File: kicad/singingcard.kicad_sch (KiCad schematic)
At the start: 16 parts, among them J2 Audio_In, SW1 Button, U1 ISD3900FYI, U2 W25Q16JVSSIQ

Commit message: Fix global label orientation - flags point toward component
- Remove incorrect 180° flip from label angle calculation
- Label flags now point toward component (same direction as pin angle)
- Left-side pins: flag points right, text extends left
- Right-side pins: flag points left, text extends right
- Wires connect to flag tip, not through label text

🤖 Generated with [Claude Code](https://claude.com/claude-code)

Co-Authored-By: Claude <noreply@anthropic.com>
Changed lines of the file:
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@@
 		(instances
 			(project "singingcard"
-				(path "/7b994266-04b8-4378-91cb-6096748c65af"
+				(path "/6c95bb3a-6328-4d30-b137-739b35f84dae"
 					(reference "U1")
 					(unit 1)
@@
 		(instances
 			(project "singingcard"
-				(path "/7b994266-04b8-4378-91cb-6096748c65af"
+				(path "/6c95bb3a-6328-4d30-b137-739b35f84dae"
 					(reference "U2")
 					(unit 1)
@@
 		(instances
 			(project "singingcard"
-				(path "/7b994266-04b8-4378-91cb-6096748c65af"
+				(path "/6c95bb3a-6328-4d30-b137-739b35f84dae"
 					(reference "BT1")
 					(unit 1)
@@
 		(instances
 			(project "singingcard"
-				(path "/7b994266-04b8-4378-91cb-6096748c65af"
+				(path "/6c95bb3a-6328-4d30-b137-739b35f84dae"
 					(reference "R1")
 					(unit 1)
@@
 		(instances
 			(project "singingcard"
-				(path "/7b994266-04b8-4378-91cb-6096748c65af"
+				(path "/6c95bb3a-6328-4d30-b137-739b35f84dae"
 					(reference "R2")
 					(unit 1)
@@
 		(instances
 			(project "singingcard"
-				(path "/7b994266-04b8-4378-91cb-6096748c65af"
+				(path "/6c95bb3a-6328-4d30-b137-739b35f84dae"
 					(reference "R3")
 					(unit 1)
@@
 		(instances
 			(project "singingcard"
-				(path "/7b994266-04b8-4378-91cb-6096748c65af"
+				(path "/6c95bb3a-6328-4d30-b137-739b35f84dae"
 					(reference "R4")
 					(unit 1)
@@
 		(instances
 			(project "singingcard"
-				(path "/7b994266-04b8-4378-91cb-6096748c65af"
+				(path "/6c95bb3a-6328-4d30-b137-739b35f84dae"
 					(reference "C1")
 					(unit 1)
@@
 		(instances
 			(project "singingcard"
-				(path "/7b994266-04b8-4378-91cb-6096748c65af"
+				(path "/6c95bb3a-6328-4d30-b137-739b35f84dae"
 					(reference "C2")
 					(unit 1)
@@
 		(instances
 			(project "singingcard"
-				(path "/7b994266-04b8-4378-91cb-6096748c65af"
+				(path "/6c95bb3a-6328-4d30-b137-739b35f84dae"
 					(reference "C3")
 					(unit 1)
@@
 		(instances
 			(project "singingcard"
-				(path "/7b994266-04b8-4378-91cb-6096748c65af"
+				(path "/6c95bb3a-6328-4d30-b137-739b35f84dae"
 					(reference "C4")
 					(unit 1)
@@
 		(instances
 			(project "singingcard"
-				(path "/7b994266-04b8-4378-91cb-6096748c65af"
+				(path "/6c95bb3a-6328-4d30-b137-739b35f84dae"
 					(reference "C5")
 					(unit 1)
@@
 		(instances
 			(project "singingcard"
-				(path "/7b994266-04b8-4378-91cb-6096748c65af"
+				(path "/6c95bb3a-6328-4d30-b137-739b35f84dae"
 					(reference "C6")
 					(unit 1)
@@
 		(instances
 			(project "singingcard"
-				(path "/7b994266-04b8-4378-91cb-6096748c65af"
+				(path "/6c95bb3a-6328-4d30-b137-739b35f84dae"
 					(reference "LS1")
 					(unit 1)
@@
 		(instances
 			(project "singingcard"
-				(path "/7b994266-04b8-4378-91cb-6096748c65af"
+				(path "/6c95bb3a-6328-4d30-b137-739b35f84dae"
 					(reference "J2")
 					(unit 1)
@@
 		(instances
 			(project "singingcard"
-				(path "/7b994266-04b8-4378-91cb-6096748c65af"
+				(path "/6c95bb3a-6328-4d30-b137-739b35f84dae"
 					(reference "SW1")
 					(unit 1)
@@
 	(global_label "+3V"
 		(shape bidirectional)
-		(at 157.48 156.21 180)
+		(at 157.48 156.21 0)
 		(effects
 			(font
@@
 	(global_label "+3V"
 		(shape bidirectional)
-		(at 144.78 153.67 180)
+		(at 144.78 153.67 0)
 		(effects
 			(font
@@
 	(global_label "+3V"
 		(shape bidirectional)
-		(at 182.88 130.81 180)
+		(at 182.88 130.81 0)
 		(effects
 			(font
@@
 	(global_label "+3V"
 		(shape bidirectional)
-		(at 347.98 123.19 0)
+		(at 347.98 123.19 180)
 		(effects
 			(font
@@
 	(global_label "+3V"
 		(shape bidirectional)
-		(at 274.32 118.11 180)
+		(at 274.32 118.11 0)
 		(effects
 			(font
@@
 	(global_label "+3V"
 		(shape bidirectional)
-		(at 386.08 120.65 0)
+		(at 386.08 120.65 180)
 		(effects
 			(font
@@
 	(global_label "GND"
 		(shape bidirectional)
-		(at 182.88 140.97 180)
+		(at 182.88 140.97 0)
 		(effects
 			(font
@@
 	(global_label "GND"
 		(shape bidirectional)
-		(at 312.42 115.57 180)
+		(at 312.42 115.57 0)
 		(effects
 			(font
@@
 	(global_label "GPIO0"
 		(shape bidirectional)
-		(at 170.18 128.27 180)
+		(at 170.18 128.27 0)
 		(effects
 			(font
@@
 	(global_label "GPIO1"
 		(shape bidirectional)
-		(at 256.54 125.73 0)
+		(at 256.54 125.73 180)
 		(effects
 			(font
@@
 	(global_label "GPIO2"
 		(shape bidirectional)
-		(at 256.54 135.89 0)
+		(at 256.54 135.89 180)
 		(effects
 			(font
@@
 	(global_label "RESET"
 		(shape bidirectional)
-		(at 182.88 151.13 180)
+		(at 182.88 151.13 0)
 		(effects
 			(font
@@
 	(global_label "SPI_CS"
 		(shape bidirectional)
-		(at 243.84 153.67 0)
+		(at 243.84 153.67 180)
 		(effects
 			(font
@@
 	(global_label "SPI_CS"
 		(shape bidirectional)
-		(at 299.72 123.19 180)
+		(at 299.72 123.19 0)
 		(effects
 			(font
@@
 	(global_label "SPI_MOSI"
 		(shape bidirectional)
-		(at 256.54 166.37 0)
+		(at 256.54 166.37 180)
 		(effects
 			(font
@@
 	(global_label "SPI_MOSI"
 		(shape bidirectional)
-		(at 360.68 115.57 0)
+		(at 360.68 115.57 180)
 		(effects
 			(font
@@
 	(global_label "SPI_MISO"
 		(shape bidirectional)
-		(at 218.44 168.91 0)
+		(at 218.44 168.91 180)
 		(effects
 			(font
@@
 	(global_label "SPI_MISO"
 		(shape bidirectional)
-		(at 287.02 120.65 180)
+		(at 287.02 120.65 0)
 		(effects
 			(font
@@
 	(global_label "SPI_CLK"
 		(shape bidirectional)
-		(at 218.44 138.43 0)
+		(at 218.44 138.43 180)
 		(effects
 			(font
@@
 	(global_label "SPI_CLK"
 		(shape bidirectional)
-		(at 373.38 118.11 0)
+		(at 373.38 118.11 180)
 		(effects
 			(font
@@
 	(global_label "SP+"
 		(shape bidirectional)
-		(at 170.18 138.43 180)
+		(at 170.18 138.43 0)
 		(effects
 			(font
@@
 	(global_label "SP-"
 		(shape bidirectional)
-		(at 157.48 135.89 180)
+		(at 157.48 135.89 0)
 		(effects
 			(font
@@
 	(global_label "ANA_IN+"
 		(shape bidirectional)
-		(at 157.48 146.05 180)
+		(at 157.48 146.05 0)
 		(effects
 			(font
@@
 	(global_label "ANA_IN-"
 		(shape bidirectional)
-		(at 144.78 143.51 180)
-		(effects
-			(font
+		(at 144.78 143.51 0)
+		(effects
+			(font

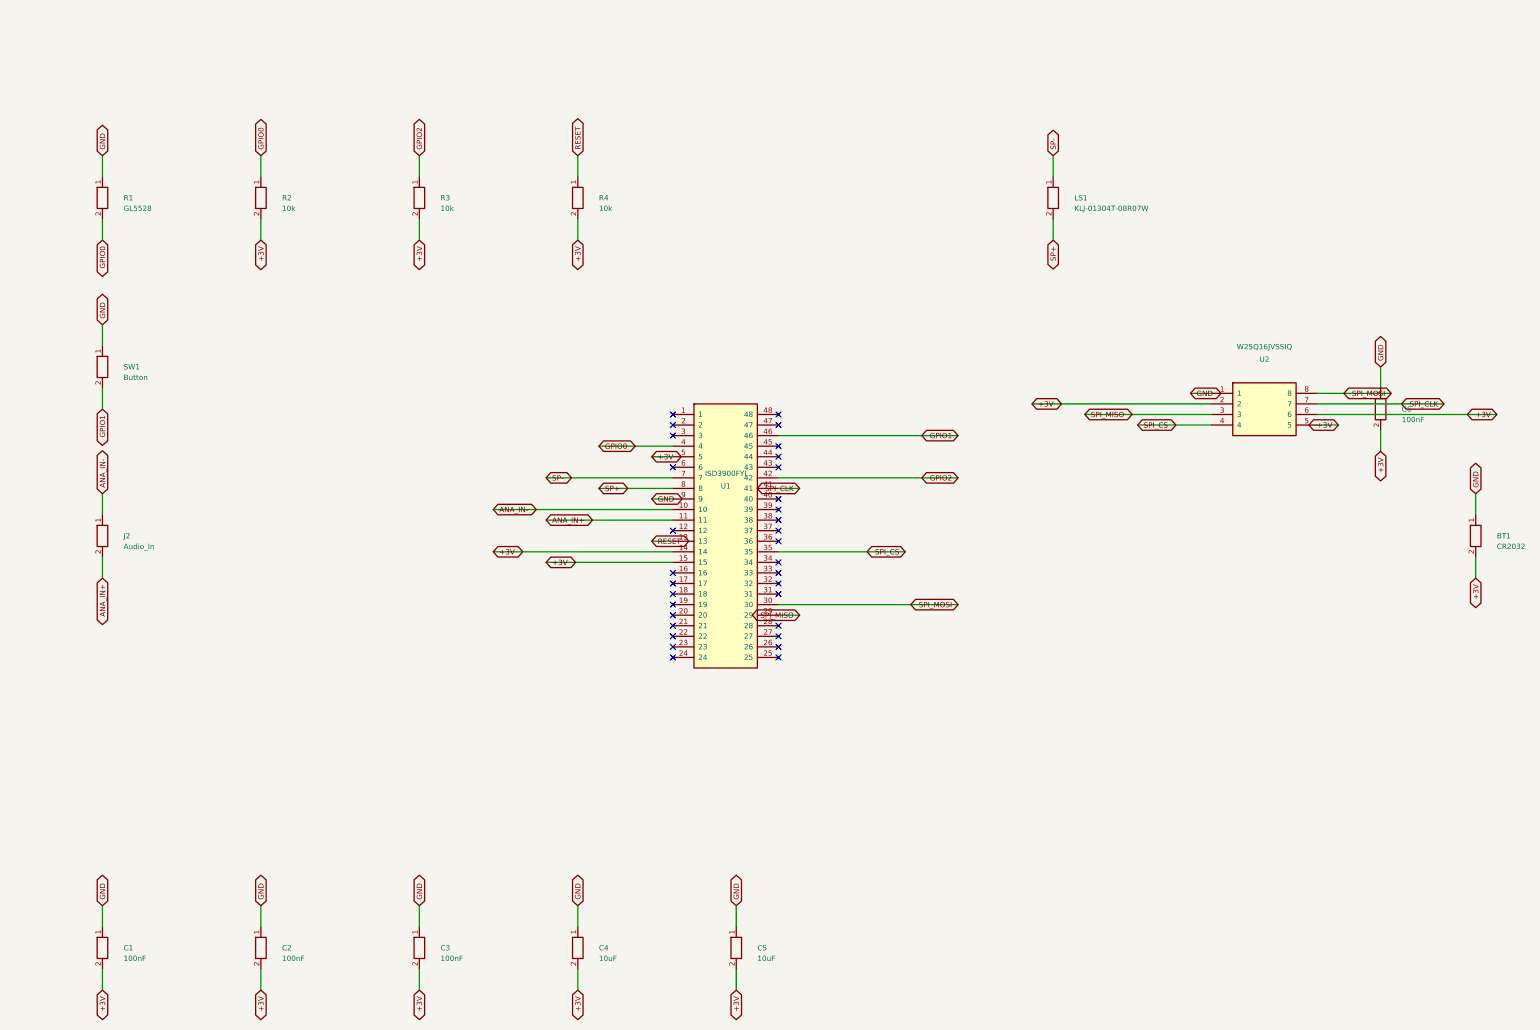
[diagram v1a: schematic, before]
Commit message: Compact schematic layout on A4, labels directly on pins
- Change from A3 to A4 page size
- Compact component positions for tighter layout
- Place labels directly at pin positions (no wires)
- Label angles opposite to pin direction so text extends away from components
- Much cleaner appearance without wire-through-label issues

🤖 Generated with [Claude Code](https://claude.com/claude-code)

Co-Authored-By: Claude <noreply@anthropic.com>
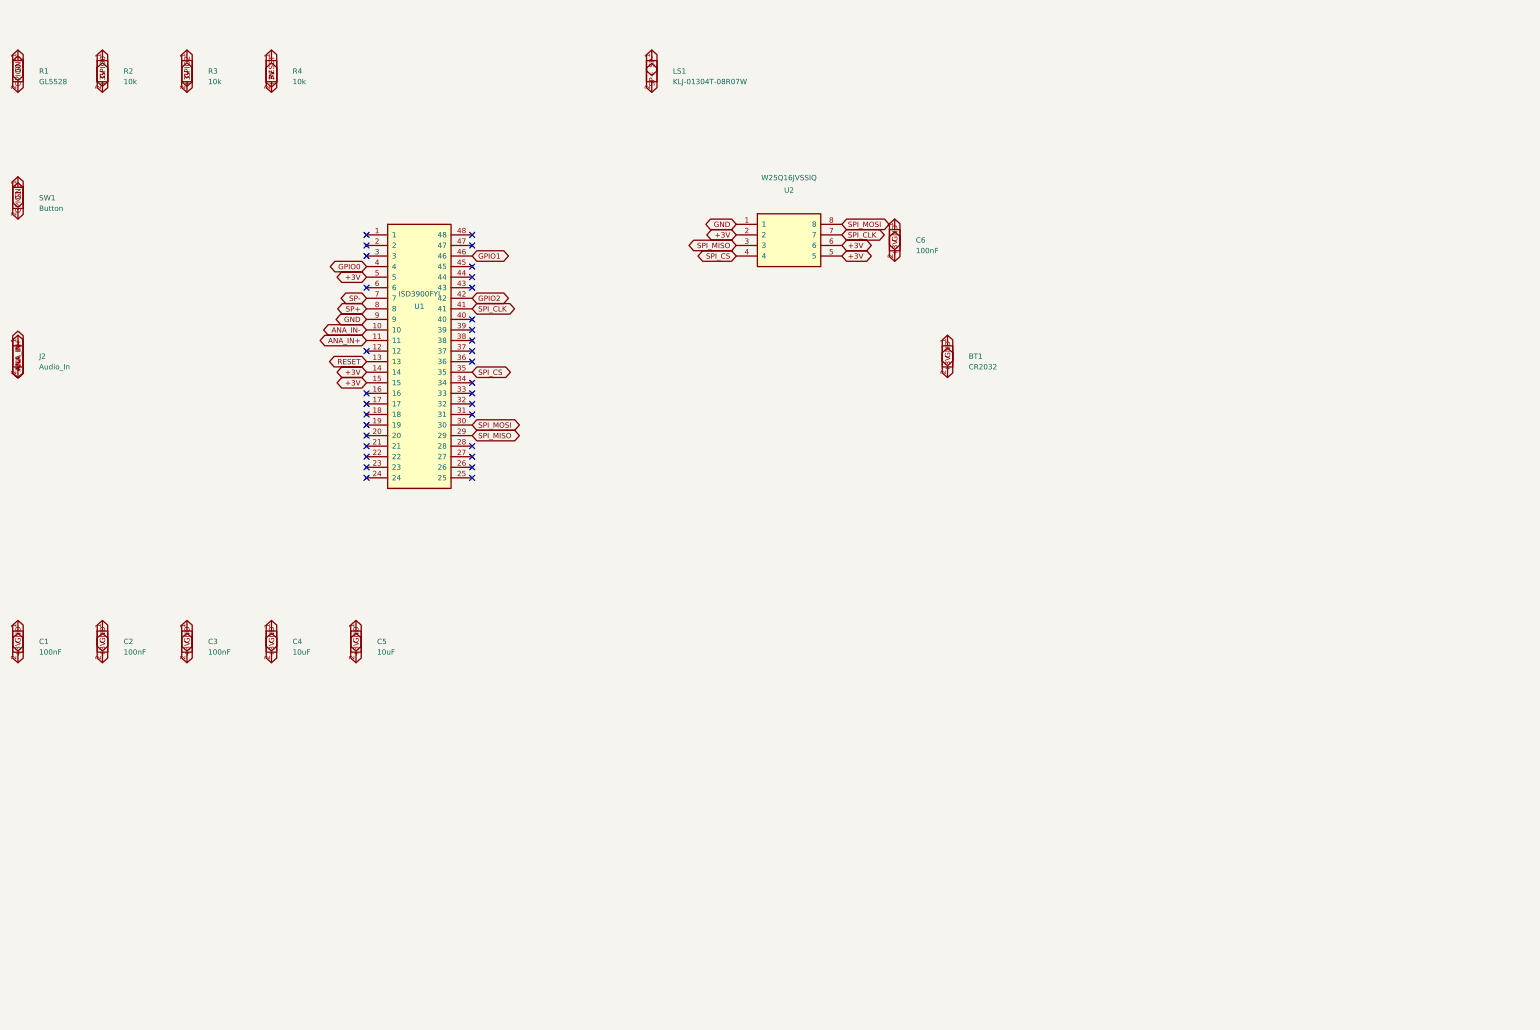
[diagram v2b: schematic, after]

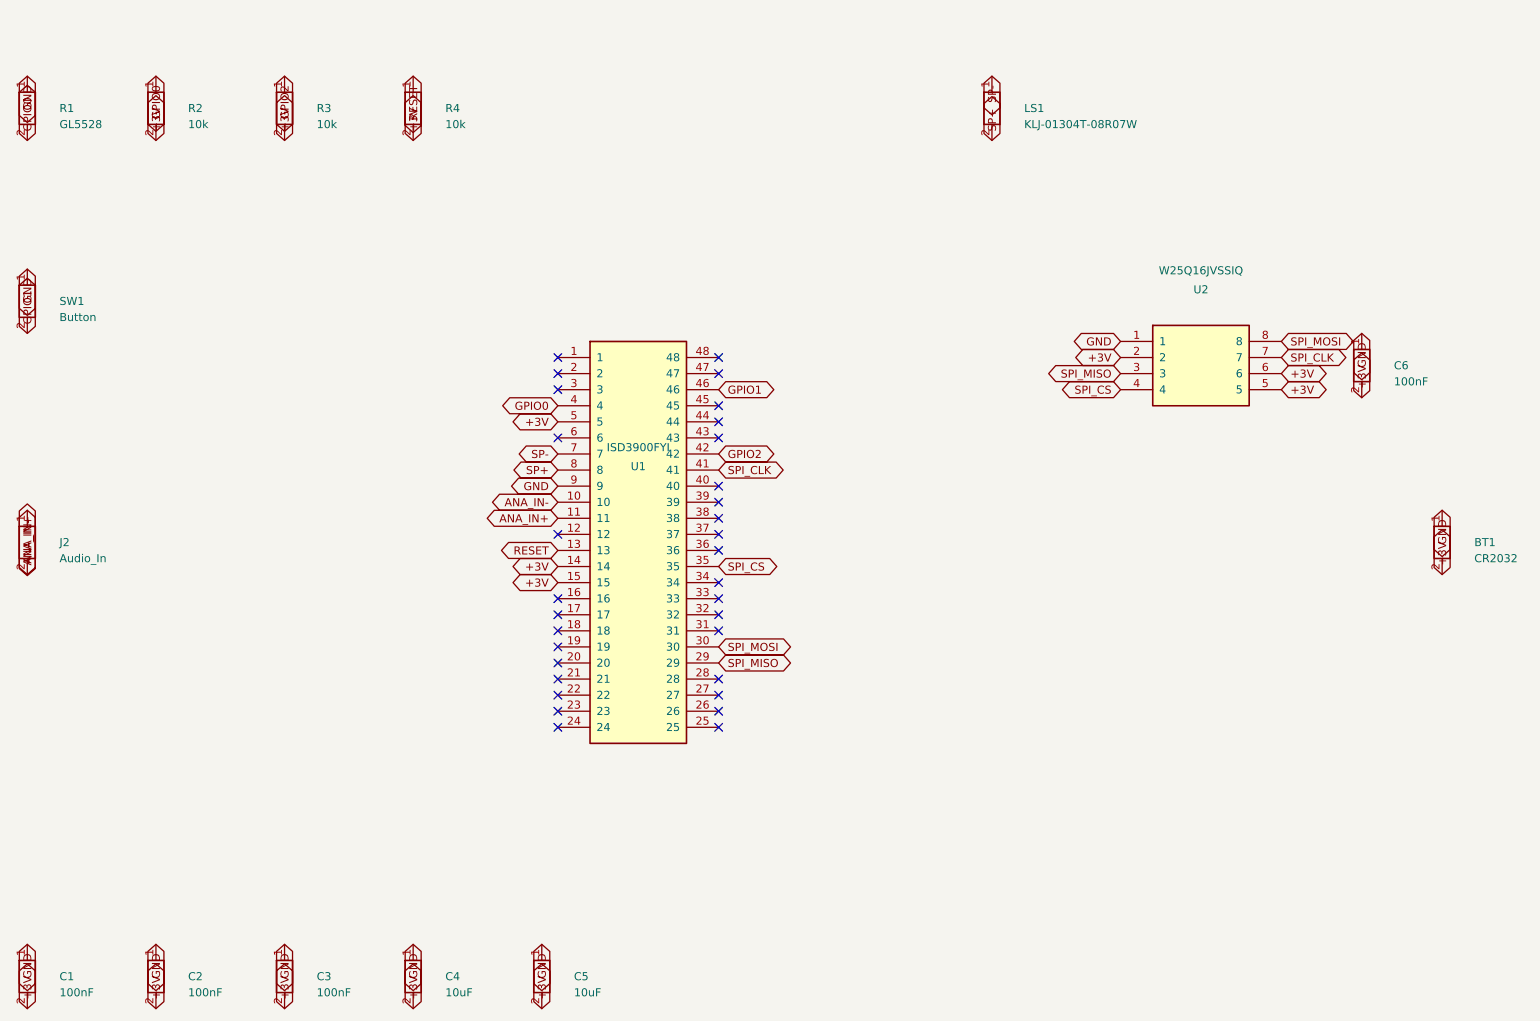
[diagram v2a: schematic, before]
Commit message: Use input shape labels with fields_autoplaced
- Change label shape from bidirectional to input
- Add fields_autoplaced yes for automatic positioning
- Add justify left to effects
- Cleaner arrow-style labels matching KiCad convention

🤖 Generated with [Claude Code](https://claude.com/claude-code)

Co-Authored-By: Claude <noreply@anthropic.com>
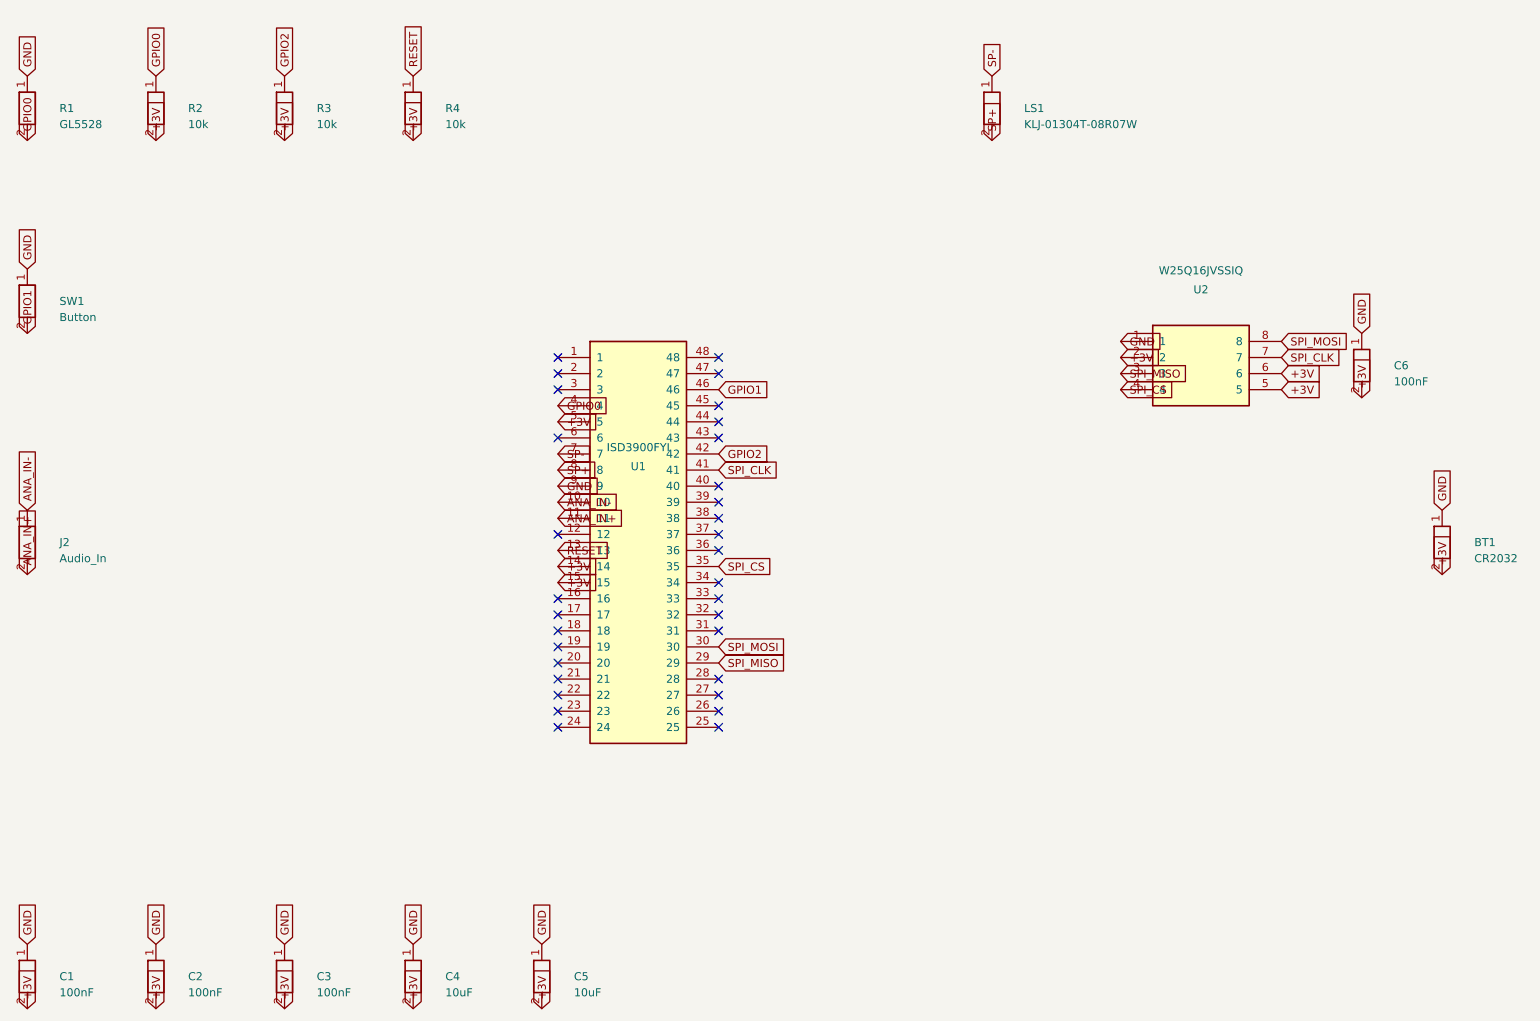
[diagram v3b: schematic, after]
